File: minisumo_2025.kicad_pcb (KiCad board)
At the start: 4 copper layers, 40.1 x 90 mm, 90 parts, among them J1 USB_C Connector, J10 DISTANCE_R90, J11 DISTANCE_R, J12 DISTANCE_RF, J13 DISTANCE_L90, J14 DISTANCE_L, J15 LINE_LEFT, J16 DISTANCE_LF, J2 SERVO, J3 START_MODULE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

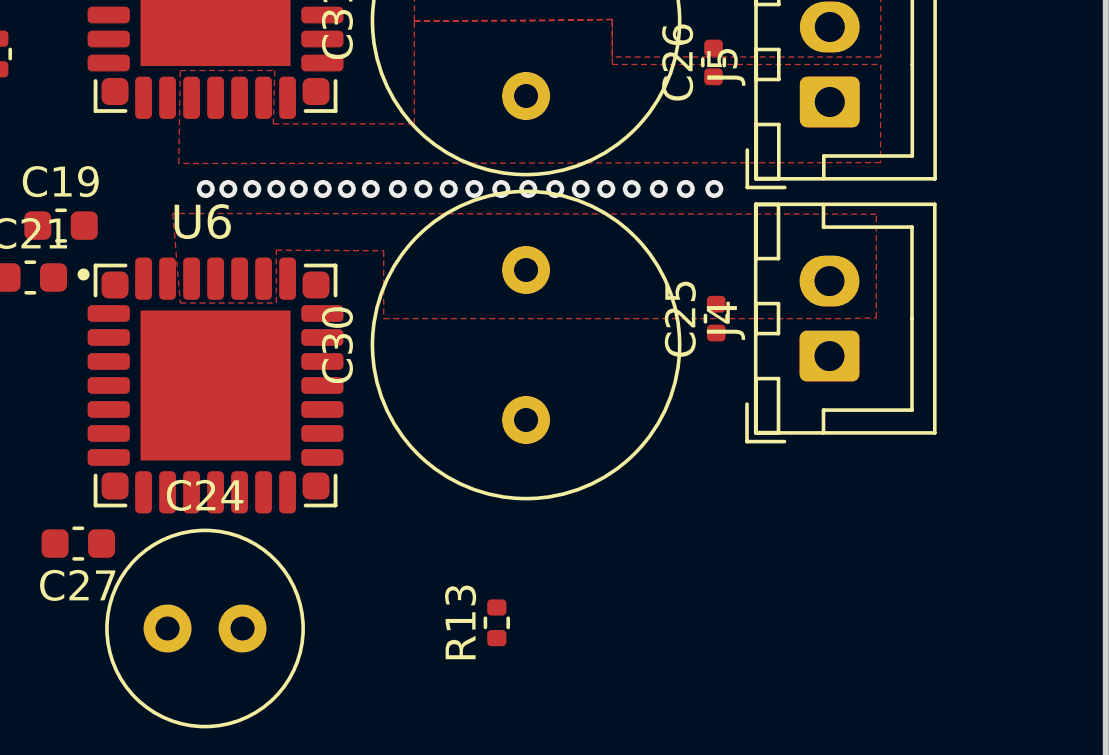
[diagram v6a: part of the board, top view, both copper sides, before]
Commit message: more driver traces
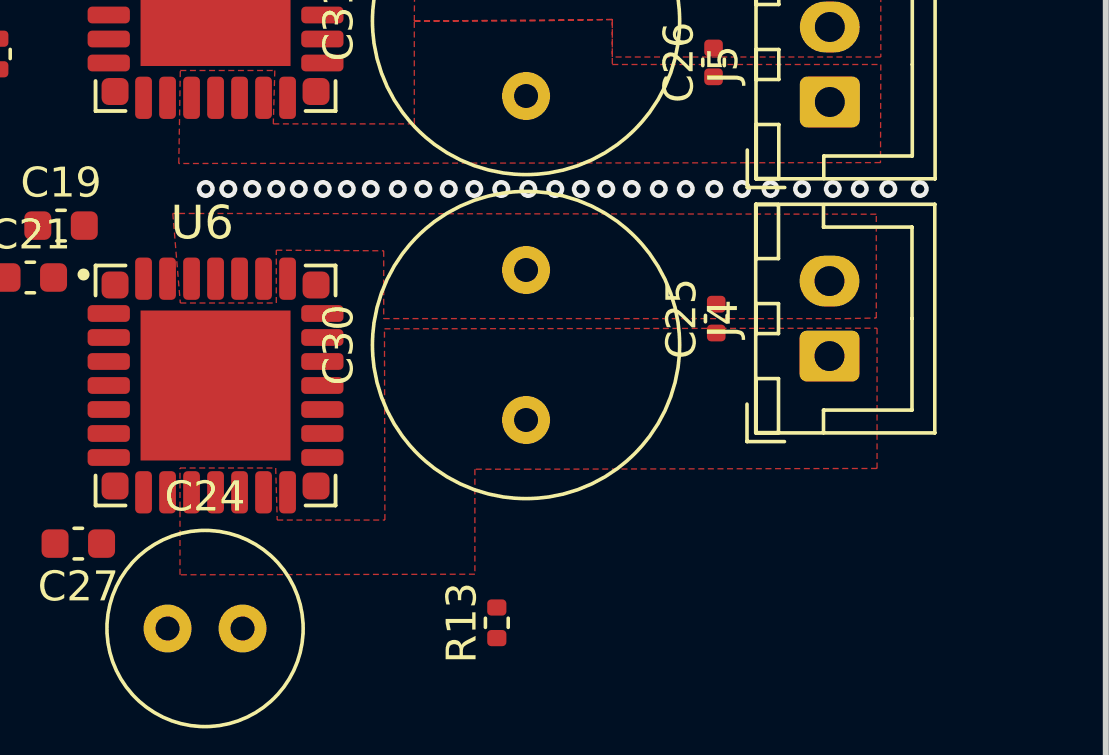
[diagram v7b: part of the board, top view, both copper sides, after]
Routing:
- net GND: vias 24 -> 31
- added copper zone on F.Cu, net /MOTOR1_A
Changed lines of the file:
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@@
+	)
+	(via
+		(at 141.4 68.1)
+		(size 0.6)
+		(drill 0.3)
+		(layers "F.Cu" "B.Cu")
+		(free yes)
+		(net 1)
 	)
 	(via
@@
 	)
 	(via
+		(at 140.375 68.1)
+		(size 0.6)
+		(drill 0.3)
+		(layers "F.Cu" "B.Cu")
+		(free yes)
+		(net 1)
+	)
+	(via
 		(at 136.5 68.1)
 		(size 0.6)
@@
 	)
 	(via
+		(at 142.3 68.1)
+		(size 0.6)
+		(drill 0.3)
+		(layers "F.Cu" "B.Cu")
+		(free yes)
+		(net 1)
+	)
+	(via
 		(at 120.5 68.1)
 		(size 0.6)
@@
 	)
 	(via
+		(at 138.375 68.1)
+		(size 0.6)
+		(drill 0.3)
+		(layers "F.Cu" "B.Cu")
+		(free yes)
+		(net 1)
+	)
+	(via
 		(at 122.85 68.1)
 		(size 0.6)
@@
 	)
 	(via
+		(at 144.3 68.1)
+		(size 0.6)
+		(drill 0.3)
+		(layers "F.Cu" "B.Cu")
+		(free yes)
+		(net 1)
+	)
+	(via
 		(at 125.2 68.1)
 		(size 0.6)
@@
 	(via
 		(at 124.4 68.1)
+		(size 0.6)
+		(drill 0.3)
+		(layers "F.Cu" "B.Cu")
+		(free yes)
+		(net 1)
+	)
+	(via
+		(at 143.25 68.1)
+		(size 0.6)
+		(drill 0.3)
+		(layers "F.Cu" "B.Cu")
+		(free yes)
+		(net 1)
+	)
+	(via
+		(at 139.325 68.1)
 		(size 0.6)
 		(drill 0.3)
@@
 			)
 		)
+	)
+	(zone
+		(net 79)
+		(net_name "/MOTOR1_A")
+		(layer "F.Cu")
+		(hatch edge 0.5)
+		(priority 7)
+		(connect_pads yes
+			(clearance 0.5)
+		)
+		(min_thickness 0.25)
+		(filled_areas_thickness no)
+		(fill yes
+			(thermal_gap 0.5)
+			(thermal_bridge_width 0.5)
+			(island_removal_mode 1)
+			(island_area_min 10)
+		)
+		(polygon
+			(pts
+				(xy 119.64 77.400092) (xy 122.83 77.400092) (xy 122.88 79.135092) (xy 126.47 79.135092) (xy 126.455 72.760092)
+				(xy 142.875 72.740092) (xy 142.875 77.415092) (xy 131.3 77.440092) (xy 129.47 77.440092) (xy 129.47 80.940092)
+				(xy 119.64 80.960092)
+			)
+		)

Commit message: more routing
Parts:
- removed C30, C31: 470uF, Capacitor_THT:C_Radial_D10.0mm_H16.0mm_P5.00mm
- C14, C15, U4: moved to F.Cu
- J6: footprint Connector_Wire:SolderWire-0.5sqmm_1x02_P4.8mm_D0.9mm_OD2.3mm -> Connector_AMASS:AMASS_XT30U-F_1x02_P5.0mm_Vertical
- R11, R12: moved to B.Cu
- moved R16 92.6 mm to (232.8, 45.5)
- moved R20 92.6 mm to (238.8, 45.5)
- moved R14 92.6 mm to (235.0, 45.5)
- moved R19 92.6 mm to (241.0, 45.5)
- moved R10 79.9 mm to (213.7, 44.0)
- moved R9 79.9 mm to (215.6, 44.0)
- moved JP3 49.0 mm to (144.9, 97.1), turned to 90 degrees
- moved JP4 47.9 mm to (148.4, 97.1), turned to 90 degrees
- moved JP1 42.8 mm to (144.9, 92.5), turned to 90 degrees
- moved JP2 41.3 mm to (148.4, 92.5), turned to 90 degrees
- moved JP5 37.1 mm to (144.9, 87.9), turned to 90 degrees
- moved JP6 35.1 mm to (148.4, 87.8), turned to 90 degrees
- moved JP7 32.4 mm to (144.9, 83.2), turned to 90 degrees
- moved JP8 29.8 mm to (148.3, 83.2), turned to 90 degrees
- moved C15 29.1 mm to (125.5, 110.9)
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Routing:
- net /ND2_1: track 6.23 -> 0.00 mm
- net /SLEW_1: track 6.23 -> 0.00 mm
- net /D1_1: track 6.00 -> 0.00 mm
- net /SLEW_2: track 1.77 -> 0.00 mm
- net /ND2_2: track 1.76 -> 0.00 mm
- net /D1_2: track 1.76 -> 0.00 mm
- net GND: vias 31 -> 78
- net /MOTOR2_B: vias 0 -> 42
- net /MOTOR2_A: vias 0 -> 42
- net /MOTOR1_B: vias 0 -> 42
- net /MOTOR1_A: vias 0 -> 40
- net +5V: vias 0 -> 10
- added copper zone on F.Cu, net +5V
- added copper zone on In1.Cu, net +5V
- added copper zone on In1.Cu, net /MOTOR1_A
- added copper zone on In1.Cu, net /MOTOR1_B
- added copper zone on In1.Cu, net /MOTOR2_A
- added copper zone on In1.Cu, net /MOTOR2_B
